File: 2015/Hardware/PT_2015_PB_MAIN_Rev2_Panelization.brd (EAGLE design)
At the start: 142.2 x 234.3 mm, 161 parts, among them Q1 Q_ACS711LC_SKETCH, Q11 Q_IRFS7437PbF, Q12 2N7002, Q14 Q_IRFS7437PbF, Q16 Q_IRFS7437PbF, Q18 Q_FDT86102LZ, Q20 Q_IRFS7437PbF, Q4 Q_ACS711LC, Q5 Q_ACS711LC, Q6 Q_IRFS7437PbF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

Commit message: Spaced out the boards to make it easier to cut.
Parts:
- moved C46 3.81 mm to (32.3, -51.3)
- moved D3 3.81 mm to (46.7, -56.1)
- moved F1 3.81 mm to (27.4, -61.7)
- moved IRLS3034-7P.2 3.81 mm to (43.9, -38.1)
- moved JP1 3.81 mm to (23.4, -56.1)
- moved R14 3.81 mm to (29.7, -51.3)
- moved R17 3.81 mm to (27.2, -51.3)
- moved R19 3.81 mm to (31.0, -55.4)
- moved R21 3.81 mm to (28.2, -65.8)
- moved R23 3.81 mm to (22.6, -65.8)
- moved R25 3.81 mm to (29.7, -61.7)
- moved R27 3.81 mm to (33.8, -60.2)
- moved S1 3.81 mm to (36.8, -64.5)
- moved U$22 3.81 mm to (59.7, -49.5)
- moved U$23 3.81 mm to (36.1, -52.6)
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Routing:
- added copper zone on layer 16, net N$361
- removed copper zone on layer 16, net N$357

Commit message: Fixed all of the FreeDFM errors. The Panelized board should be ready to order. I will confirm tonight and tomorrow, but the idea is that we will cut the SSR board out of the Power Board to save a ton of money.
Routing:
- net N$357: track 22.3 -> 30.4 mm
- added copper zone on layer 16, net N$357
- removed copper zone on layer 16, net N$361
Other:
- board size 142.2 x 234.3 mm -> 142.5 x 234.8 mm

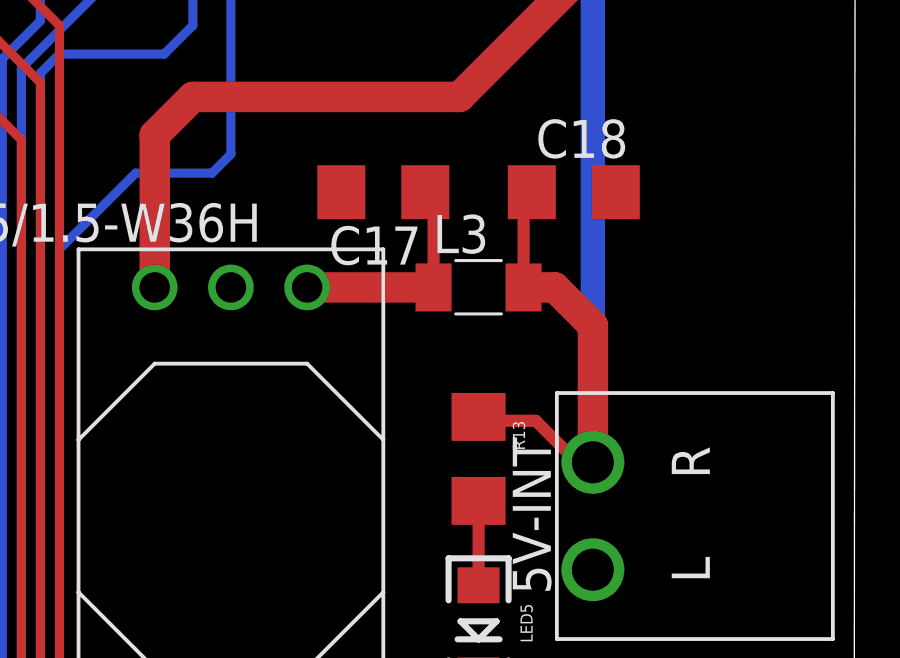
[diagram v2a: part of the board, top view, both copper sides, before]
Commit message: Fixed the Ferrite Bead Footprint
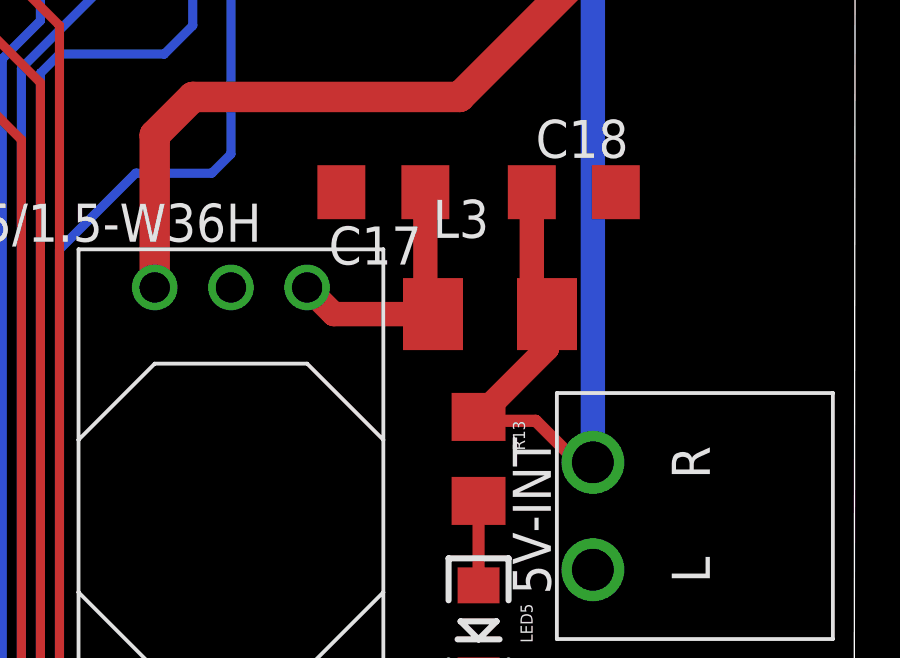
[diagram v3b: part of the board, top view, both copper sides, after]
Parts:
- L3: device resistor:L3216C -> rcl:L4532M
- moved L3 0.97 mm to (125.5, 16.3)
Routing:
- net +5V: track 627.9 -> 626.3 mm
- net N$100: track 7.50 -> 9.12 mm
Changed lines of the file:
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@@
 <element name="OKI-78SR-5/1.5-W36H" library="MRDT-2015-PowerBoard" package="OKI-78SRH" value="Q_OKI-78SR" x="116.84" y="17.145" rot="R180"/>
 <element name="C17" library="resistor" package="C1206" value="47µF" x="121.92" y="20.32" rot="R180"/>
-<element name="L3" library="resistor" package="L3216C" value="" x="125.095" y="17.145"/>
 <element name="C18" library="resistor" package="C1206" value="47µF" x="128.27" y="20.32"/>
 <element name="12V-AUX" library="MRDT-2015-PowerBoard" package="20020618-M02" value="H_20020618-M02" x="7.62" y="149.86" rot="R270"/>
@@
 <attribute name="NAME" x="36.449" y="-59.055" size="1.27" layer="25" rot="R270"/>
 </element>
+<element name="L3" library="rcl" package="L4532M" value="" x="125.476" y="16.256"/>
 </elements>
 <signals>
@@
 <contactref element="Q4" pad="8"/>
 <contactref element="Q5" pad="8"/>
-<contactref element="L3" pad="2"/>
 <contactref element="C18" pad="1"/>
 <contactref element="R13" pad="1"/>
@@
 <wire x1="33.655" y1="116.78" x2="35.37" y2="116.78" width="0.4064" layer="1"/>
 <wire x1="35.37" y1="116.78" x2="35.43" y2="116.84" width="0.4064" layer="1"/>
-<wire x1="126.595" y1="17.145" x2="127.635" y2="17.145" width="1.016" layer="1"/>
-<wire x1="127.635" y1="17.145" x2="128.905" y2="15.875" width="1.016" layer="1"/>
-<wire x1="128.905" y1="15.875" x2="128.905" y2="11.315" width="1.016" layer="1"/>
-<wire x1="126.595" y1="17.145" x2="126.595" y2="20.045" width="0.4064" layer="1"/>
 <wire x1="126.595" y1="20.045" x2="126.87" y2="20.32" width="0.4064" layer="1"/>
 <wire x1="128.905" y1="11.315" x2="128.385" y2="11.315" width="0.4064" layer="1"/>
@@
 <wire x1="42.545" y1="20.79625" x2="42.545" y2="18.99" width="0.3048" layer="1"/>
 <wire x1="8.382" y1="137.414" x2="9.398" y2="136.398" width="0.4064" layer="1"/>
+<contactref element="L3" pad="2"/>
+<wire x1="127.376" y1="16.256" x2="126.87" y2="16.762" width="0.8128" layer="1"/>
+<wire x1="126.87" y1="16.762" x2="126.87" y2="20.32" width="0.8128" layer="1"/>
+<wire x1="127.376" y1="16.256" x2="127.376" y2="15.111" width="0.8128" layer="1"/>
+<wire x1="127.376" y1="15.111" x2="125.095" y2="12.83" width="0.8128" layer="1"/>
 </signal>
 <signal name="N$3">
@@
 <contactref element="OKI-78SR-5/1.5-W36H" pad="3"/>
 <contactref element="C17" pad="1"/>
+<wire x1="123.595" y1="20.045" x2="123.32" y2="20.32" width="0.4064" layer="1"/>
 <contactref element="L3" pad="1"/>
-<wire x1="119.38" y1="17.145" x2="123.595" y2="17.145" width="1.016" layer="1"/>
-<wire x1="123.595" y1="17.145" x2="123.595" y2="20.045" width="0.4064" layer="1"/>
-<wire x1="123.595" y1="20.045" x2="123.32" y2="20.32" width="0.4064" layer="1"/>
+<wire x1="119.38" y1="17.145" x2="120.269" y2="16.256" width="0.8128" layer="1"/>
+<wire x1="120.269" y1="16.256" x2="123.576" y2="16.256" width="0.8128" layer="1"/>
+<wire x1="123.576" y1="16.256" x2="123.32" y2="16.512" width="0.8128" layer="1"/>
+<wire x1="123.32" y1="16.512" x2="123.32" y2="20.32" width="0.8128" layer="1"/>
 </signal>
 <signal name="M1-IMEAS">
